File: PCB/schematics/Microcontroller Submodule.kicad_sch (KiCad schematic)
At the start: 1 part

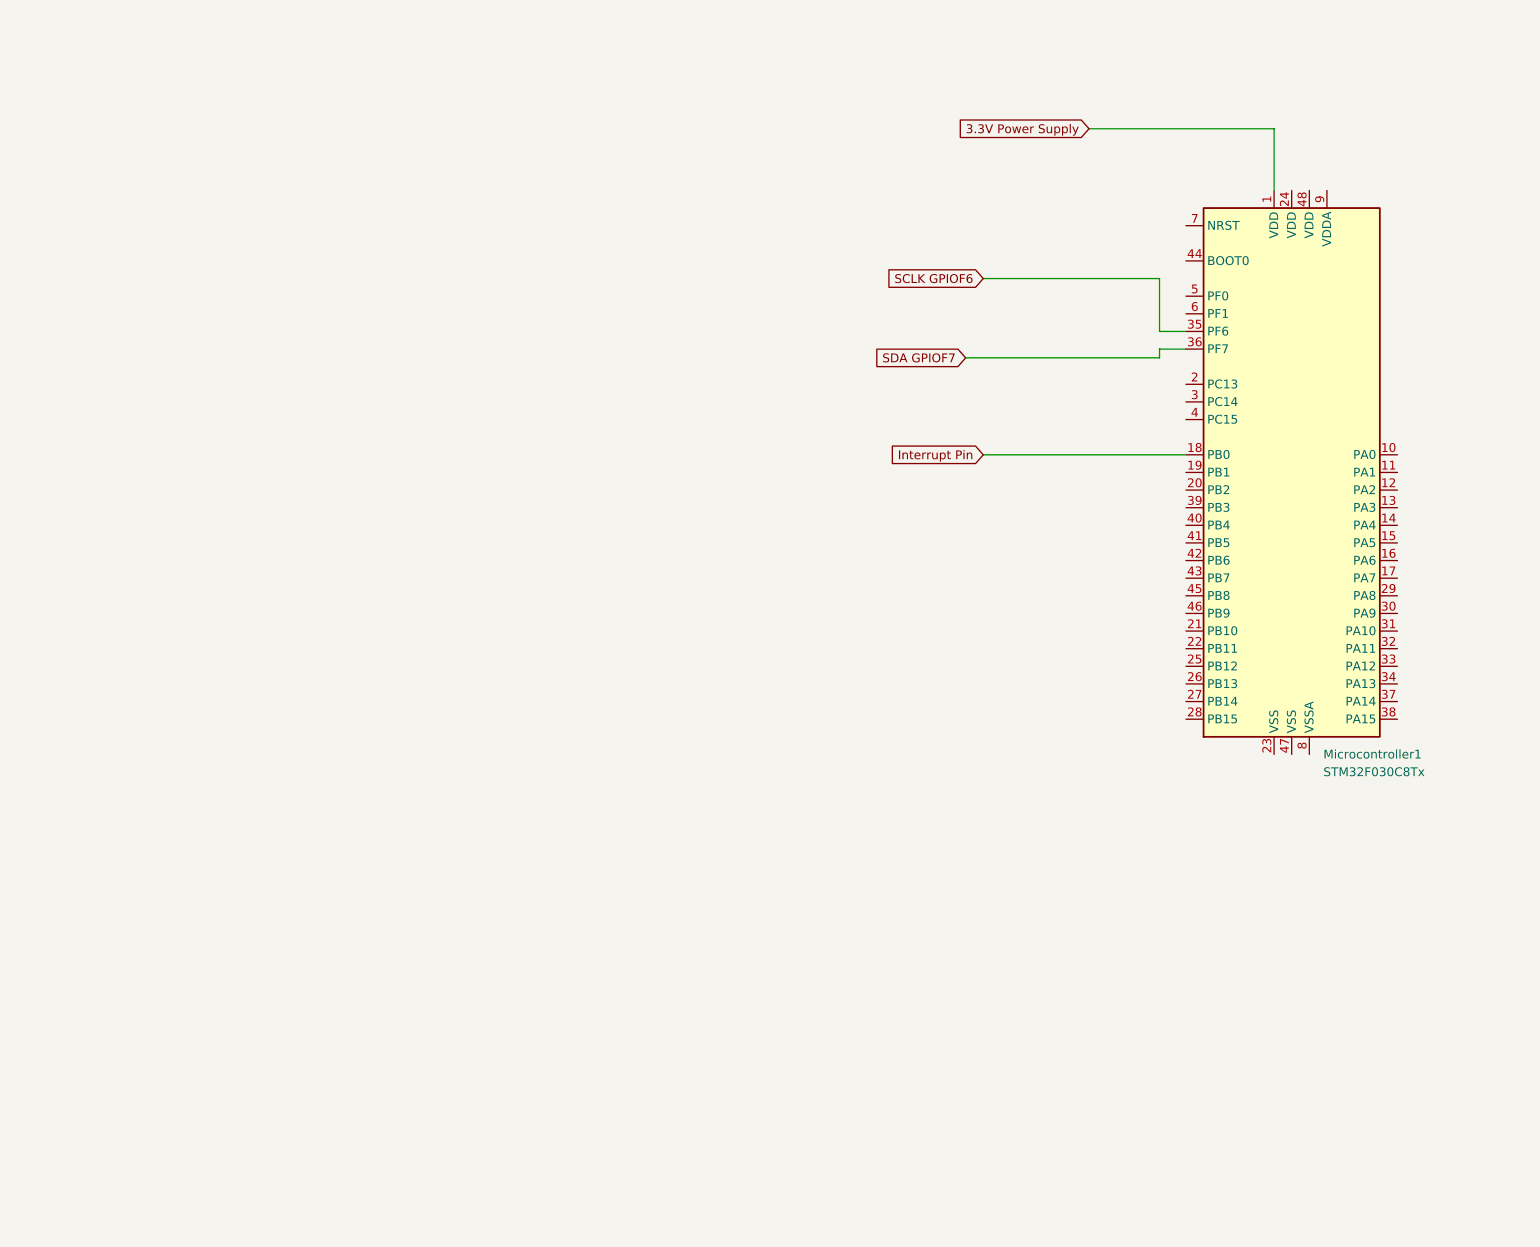
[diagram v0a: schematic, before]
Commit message: updated microcontroller schematic
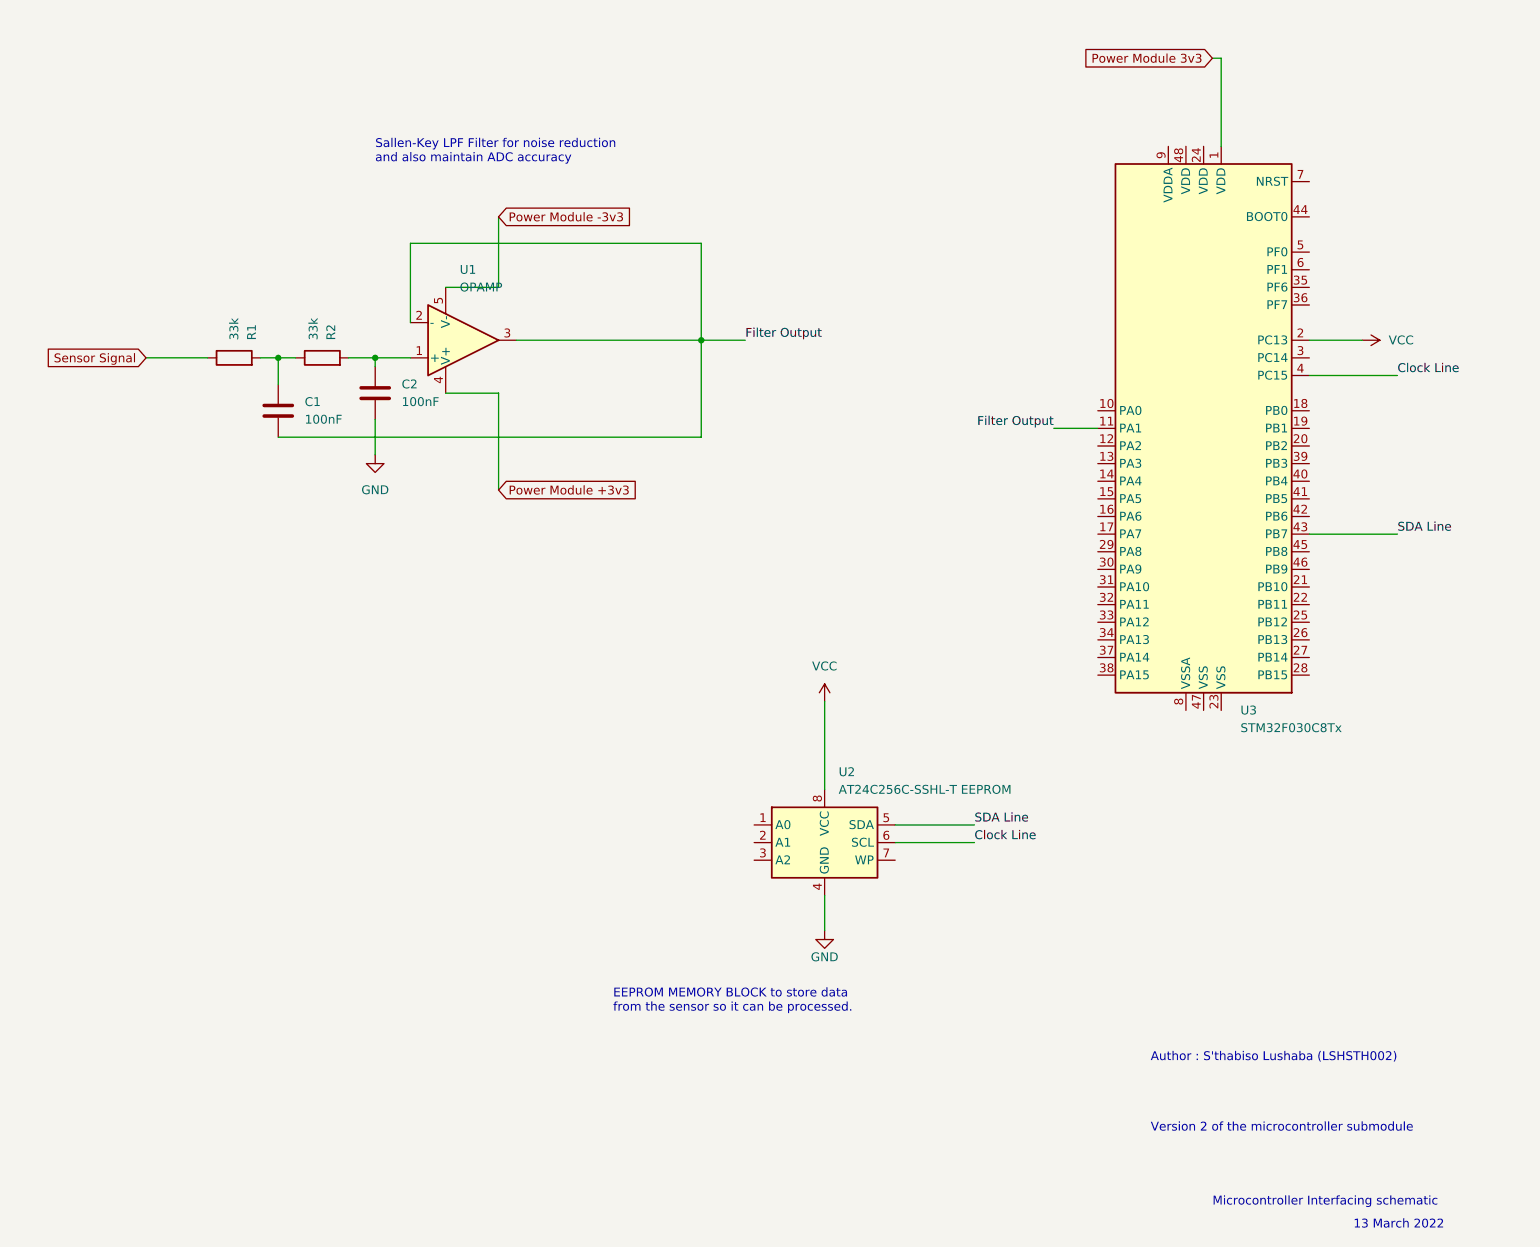
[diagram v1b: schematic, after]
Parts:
- removed Microcontroller1: STM32F030C8Tx, Package_QFP:LQFP-48_7x7mm_P0.5mm, symbol MCU_ST_STM32F0:STM32F030C8Tx
- added C1, C2: 100nF, symbol Device:C
- added R1, R2: 33k, symbol Device:R
- added U1: OPAMP, symbol pspice:OPAMP
- added U2: AT24C256C-SSHL-T EEPROM, symbol Memory_EEPROM:24LC64
- added U3: STM32F030C8Tx, Package_QFP:LQFP-48_7x7mm_P0.5mm, symbol MCU_ST_STM32F0:STM32F030C8Tx
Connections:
- new net: C1.1, R1.2, R2.1
- new net: C2.1, R2.2, U1.1 (+)
- new net Clock Line: U2.6 (SCL), U3.4 (PC15)
- new net Filter Output: C1.2, U1.2 (-), U1.3, U3.11 (PA1)
- new net GND: C2.2, U2.4 (GND)
- new net Power Module +3v3: U1.4 (V+)
- new net Power Module -3v3: U1.5 (V-)
- new net Power Module 3v3: U3.1 (VDD)
- new net SDA Line: U2.5 (SDA), U3.43 (PB7)
- new net Sensor Signal: R1.1
- new net VCC: U2.8 (VCC), U3.2 (PC13)
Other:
- note added: "13 March 2022"
- note added: "Author : S'thabiso Lushaba (LSHSTH002)"
- note added: "EEPROM MEMORY BLOCK to store data from the sensor so it can be processed."
- note added: "Microcontroller Interfacing schematic"
- note added: "Sallen-Key LPF Filter for noise reduction and also maintain ADC accuracy"
- note added: "Version 2 of the microcontroller submodule"

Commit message: updated microcontroller schematic
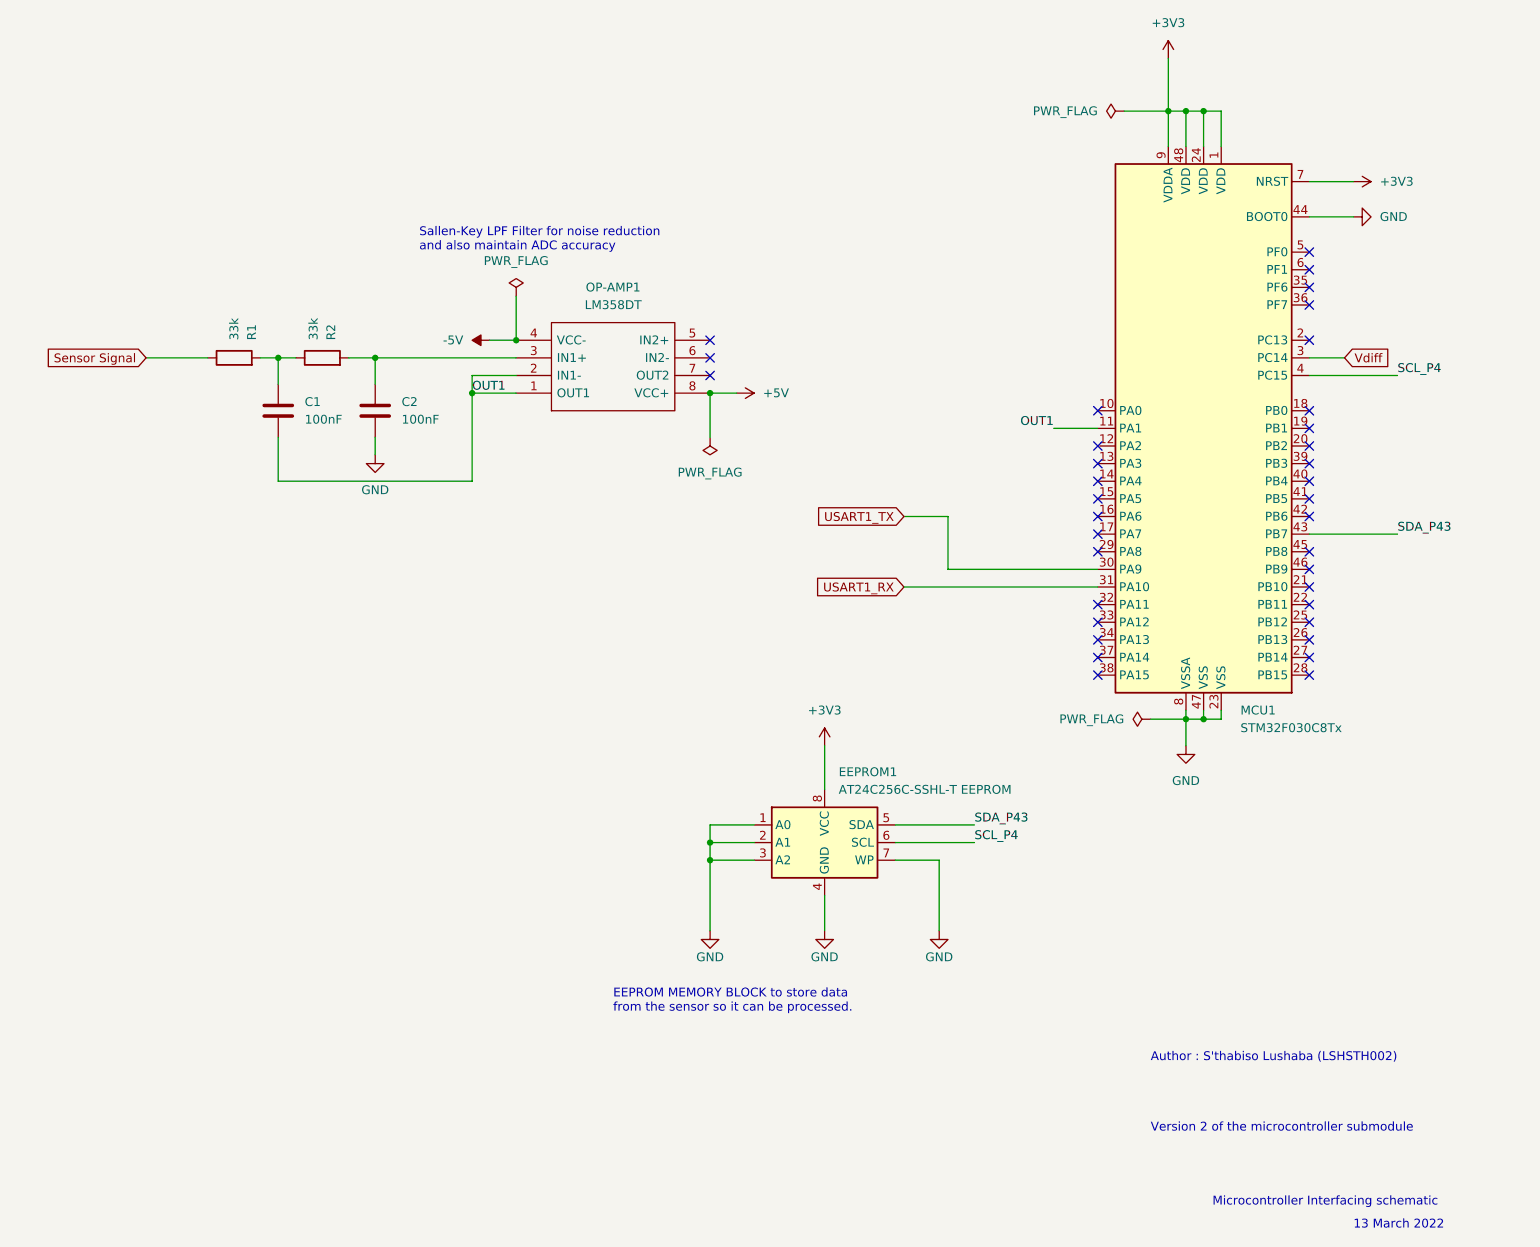
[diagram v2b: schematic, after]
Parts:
- removed U1: OPAMP, symbol pspice:OPAMP
- added OP-AMP1: LM358DT, SOIC127P600X175-8N, symbol LM358DT:LM358DT
- C1, C2: JLCPCB Part CC2A104ZC1ID3F7C30MF -> C254109; Manufacturer_Part_Number (none) -> CC2A104ZC1ID3F7C30MF
- EEPROM1: renamed from U2; Manufacturer_Part_Number (none) -> AT24C256C-SSHL-T
- R1, R2: JLCPCB Part 4D02WGF3302TCE -> C425317; Manufacturer_Part_Number (none) -> 4D02WGF3302TCE
- renumbered U3 to MCU1
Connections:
- net Power Module 3v3 is gone; now on net +3V3: MCU1.1 (VDD)
- net GND: now also EEPROM1.1 (A0), EEPROM1.2 (A1), EEPROM1.3 (A2), EEPROM1.7 (WP), MCU1.23 (VSS), MCU1.44 (BOOT0), MCU1.47 (VSS), MCU1.8 (VSSA)
- net +3V3: now reaches MCU1.24 (VDD)
- net +3V3: now also EEPROM1.8 (VCC), MCU1.48 (VDD), MCU1.7 (NRST), MCU1.9 (VDDA)
- net Vdiff: now reaches MCU1.3 (PC14)
- net USART1_TX: now reaches MCU1.30 (PA9)
- net USART1_RX: now reaches MCU1.31 (PA10)
- net at C2.1, R2.2: now also OP-AMP1.3 (IN1+)
- net Clock Line renamed SCL_P4
- net Filter Output renamed OUT1
- net OUT1: now also OP-AMP1.1 (OUT1), OP-AMP1.2 (IN1-)
- net SDA Line renamed SDA_P43
- net VCC: no longer names the net of MCU1.2 (PC13)
- net VCC: no longer EEPROM1.8 (VCC)
- new net +5V: OP-AMP1.8 (VCC+)
- new net -5V: OP-AMP1.4 (VCC-)
- no-connect marks 0 -> 36
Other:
- moved on the sheet: C2
